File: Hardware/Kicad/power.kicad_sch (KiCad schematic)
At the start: 24 parts, among them J1 PinHeader_01x05_P2.54mm_Verti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, J10 LED Strips Output, J12 Enclosure Power, J13 PCB Power, J2 PinHeader_01x05_P2.54mm_Verti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, J21 5V/10A Adapter, J9 Power In, P1 IEC_60320_C13_Plug, U1 AMS1117-3.3

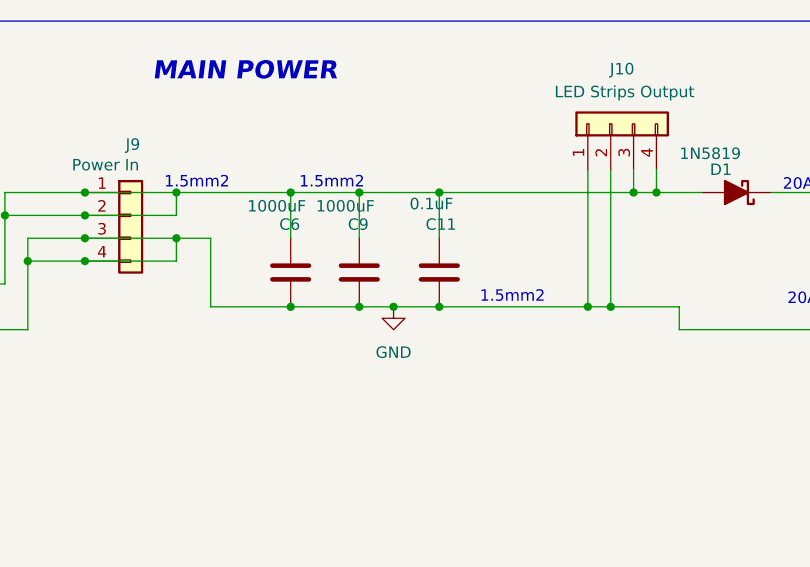
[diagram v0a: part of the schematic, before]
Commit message: Added safety in Kicad power, added NVS read version/tm1637 brightness
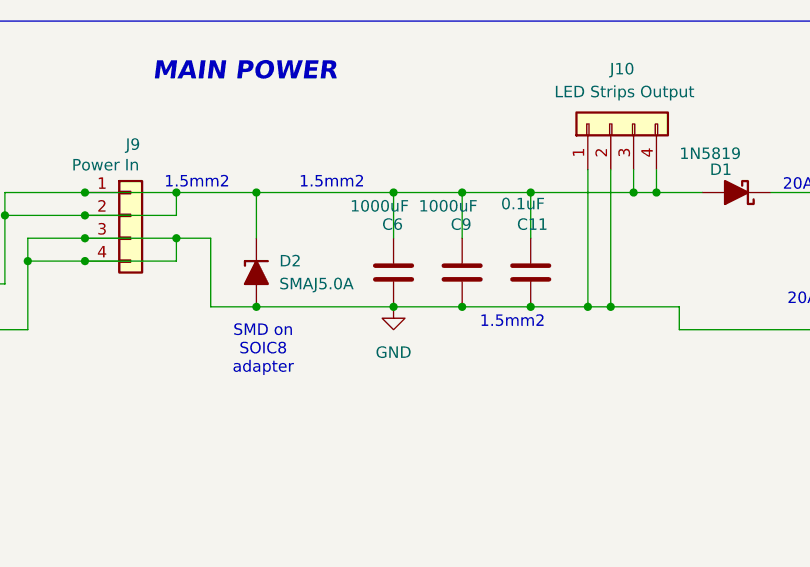
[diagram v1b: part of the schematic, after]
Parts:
- added D2: SMAJ5.0A, PCM_Diode_SMD_AKL:D_SMA, symbol PCM_Diode_TVS_AKL:SMAJ5.0A
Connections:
- net GND: now also D2.2 (A)
- net at C11.2, C6.2, C9.2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: now also D2.1 (K)
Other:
- note added: "SMD on SOIC8 adapter"
- moved on the sheet: C11, C6, C9
